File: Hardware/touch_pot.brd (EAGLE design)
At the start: 44.5 x 78.7 mm, 78 parts, among them U1 PIC16F1829, U2 AD5262, U3 5V

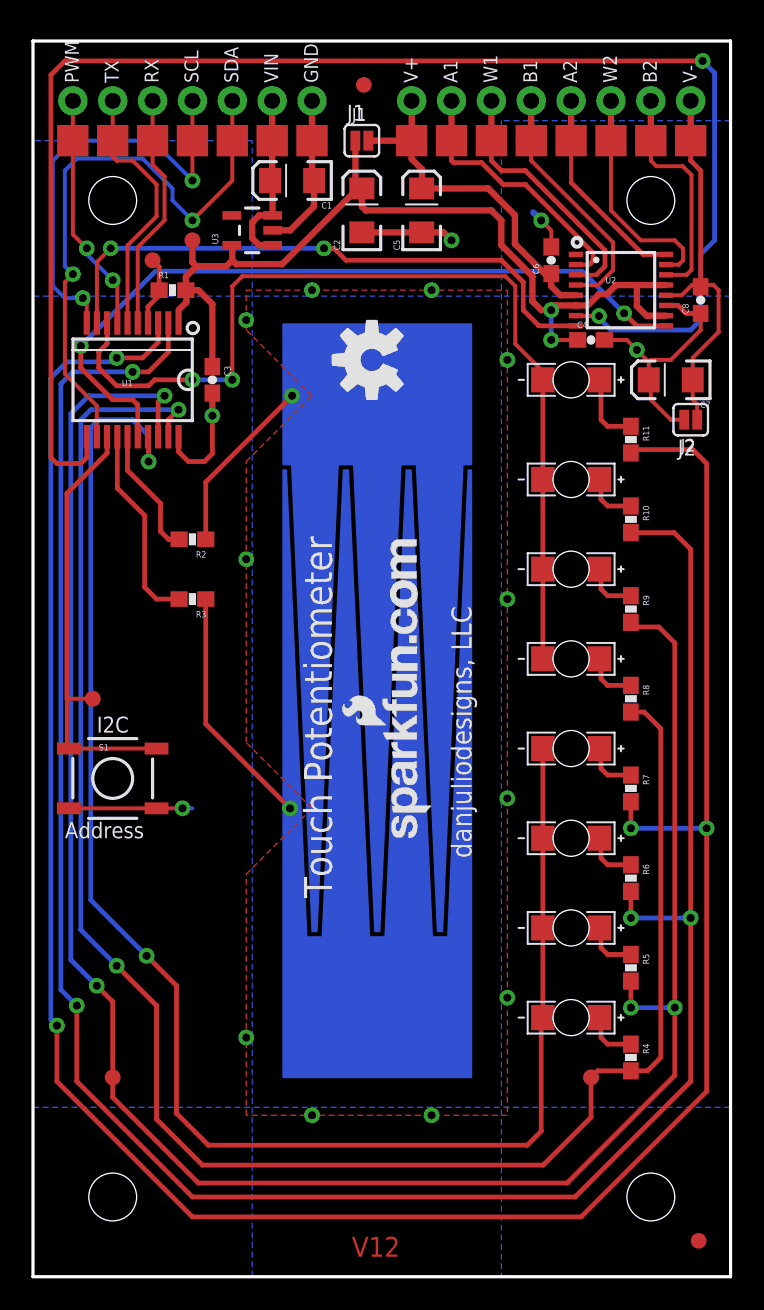
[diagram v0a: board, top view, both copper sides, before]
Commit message: V13 Changes
Adjusted headers to fit on breadboard. Minor rerouting. Moved silk.
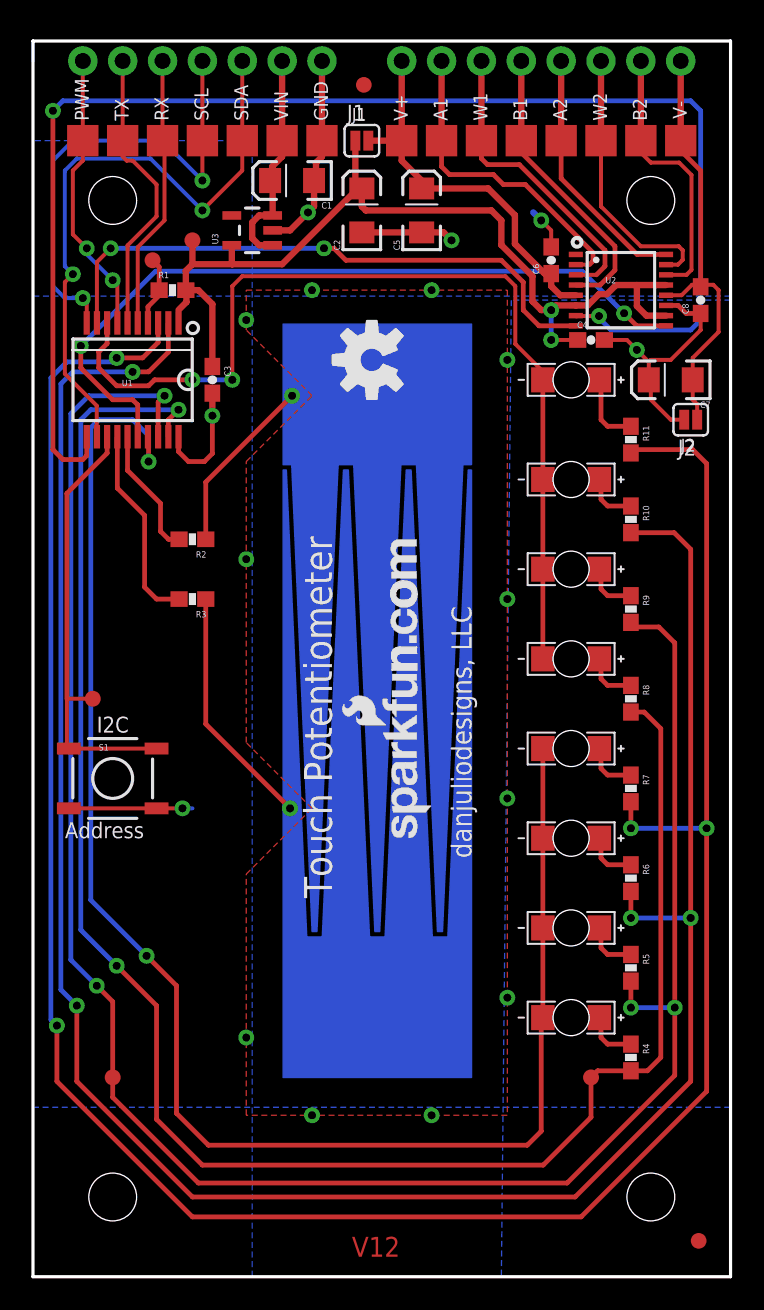
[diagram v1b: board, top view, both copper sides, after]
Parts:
- moved JP1 2.62 mm to (13.3, 77.5)
- moved JP12 2.62 mm to (31.1, 77.5)
- moved JP13 2.62 mm to (28.6, 77.5)
- moved JP14 2.62 mm to (26.0, 77.5)
- moved JP2 2.62 mm to (10.8, 77.5)
- moved JP3 2.62 mm to (3.17, 77.5)
- moved JP4 2.62 mm to (8.26, 77.5)
- moved JP5 2.62 mm to (5.71, 77.5)
- moved JP6 2.62 mm to (15.9, 77.5)
- moved JP10 2.62 mm to (36.2, 77.5)
- moved JP11 2.62 mm to (33.7, 77.5)
- moved JP15 2.62 mm to (23.5, 77.5)
- moved JP7 2.62 mm to (18.4, 77.5)
- moved JP8 2.62 mm to (41.3, 77.5)
- moved JP9 2.62 mm to (38.7, 77.5)
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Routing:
- net SCLK: track 96.1 -> 89.1 mm
- net A1: track 17.0 -> 20.4 mm
- net SCL: track 27.5 -> 30.6 mm
- net W1: track 16.5 -> 19.6 mm
- net A2: track 13.2 -> 16.2 mm
- net B1: track 15.7 -> 18.7 mm
- net W2: track 14.5 -> 17.4 mm
- net B2: track 14.6 -> 17.5 mm
- net GND: track 50.1 -> 52.9 mm, vias 16 -> 17
- net VIN: track 11.4 -> 14.2 mm
- net V-: track 25.0 -> 27.8 mm
- net PWM_OUT: track 15.3 -> 18.1 mm
- net RX: track 15.2 -> 17.5 mm
- net V+: track 22.8 -> 25.0 mm
- net TX: track 16.7 -> 18.6 mm
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
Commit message: V13
v13
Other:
- board text added: "V13"
- board text removed: "V12"
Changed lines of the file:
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@@
 <setting verticaltext="up"/>
 </settings>
-<grid distance="0.05" unitdist="inch" unit="inch" style="lines" multiple="1" display="yes" altdistance="0.005" altunitdist="inch" altunit="inch"/>
+<grid distance="0.05" unitdist="inch" unit="inch" style="lines" multiple="1" display="yes" altdistance="0.0025" altunitdist="inch" altunit="inch"/>
 <layers>
 <layer number="1" name="Top" color="4" fill="1" visible="yes" active="yes"/>
@@
 <text x="19.05" y="24.13" size="1.778" layer="21" ratio="15" rot="R90">Touch Potentiometer</text>
 <text x="27.94" y="26.67" size="1.27" layer="21" ratio="15" rot="R90">danjuliodesigns, LLC</text>
-<text x="13.716" y="73.66" size="0.889" layer="21" ratio="15" rot="R90">SDA</text>
-<text x="11.176" y="73.66" size="0.889" layer="21" ratio="15" rot="R90">SCL</text>
-<text x="3.556" y="73.66" size="0.889" layer="21" ratio="15" rot="R90">PWM</text>
-<text x="6.096" y="73.66" size="0.889" layer="21" ratio="15" rot="R90">TX</text>
-<text x="8.636" y="73.66" size="0.889" layer="21" ratio="15" rot="R90">RX</text>
-<text x="16.256" y="73.66" size="0.889" layer="21" ratio="15" rot="R90">VIN</text>
-<text x="18.796" y="73.66" size="0.889" layer="21" ratio="15" rot="R90">GND</text>
-<text x="23.876" y="73.66" size="0.889" layer="21" ratio="15" rot="R90">V+</text>
-<text x="26.416" y="73.66" size="0.889" layer="21" ratio="15" rot="R90">A1</text>
-<text x="28.956" y="73.66" size="0.889" layer="21" ratio="15" rot="R90">W1</text>
-<text x="31.496" y="73.66" size="0.889" layer="21" ratio="15" rot="R90">B1</text>
-<text x="34.036" y="73.66" size="0.889" layer="21" ratio="15" rot="R90">A2</text>
-<text x="36.576" y="73.66" size="0.889" layer="21" ratio="15" rot="R90">W2</text>
-<text x="39.116" y="73.66" size="0.889" layer="21" ratio="15" rot="R90">B2</text>
-<text x="41.656" y="73.787" size="0.889" layer="21" ratio="15" rot="R90">V-</text>
+<text x="13.716" y="73.914" size="0.889" layer="21" ratio="15" rot="R90">SDA</text>
+<text x="11.176" y="73.914" size="0.889" layer="21" ratio="15" rot="R90">SCL</text>
+<text x="3.683" y="73.914" size="0.889" layer="21" ratio="15" rot="R90">PWM</text>
+<text x="6.096" y="74.7395" size="0.889" layer="21" ratio="15" rot="R90">TX</text>
+<text x="8.6995" y="74.7395" size="0.889" layer="21" ratio="15" rot="R90">RX</text>
+<text x="16.3195" y="74.168" size="0.889" layer="21" ratio="15" rot="R90">VIN</text>
+<text x="18.8595" y="73.914" size="0.889" layer="21" ratio="15" rot="R90">GND</text>
+<text x="23.9395" y="74.7395" size="0.889" layer="21" ratio="15" rot="R90">V+</text>
+<text x="26.416" y="74.7395" size="0.889" layer="21" ratio="15" rot="R90">A1</text>
+<text x="28.956" y="74.7395" size="0.889" layer="21" ratio="15" rot="R90">W1</text>
+<text x="31.496" y="74.7395" size="0.889" layer="21" ratio="15" rot="R90">B1</text>
+<text x="34.036" y="74.7395" size="0.889" layer="21" ratio="15" rot="R90">A2</text>
+<text x="36.576" y="74.7395" size="0.889" layer="21" ratio="15" rot="R90">W2</text>
+<text x="39.116" y="74.7395" size="0.889" layer="21" ratio="15" rot="R90">B2</text>
+<text x="41.656" y="74.7395" size="0.889" layer="21" ratio="15" rot="R90">V-</text>
 <text x="53.34" y="-16.51" size="1.778" layer="51" font="vector" ratio="10">danjuliodesigns, LLC</text>
-<text x="20.32" y="1.27" size="1.27" layer="1" font="vector" ratio="15" distance="45">V12</text>
+<text x="20.32" y="1.27" size="1.27" layer="1" font="vector" ratio="15" distance="45">V13</text>
 <text x="4.064" y="34.671" size="1.016" layer="21" font="vector" ratio="15">I2C</text>
 <text x="2.032" y="27.94" size="1.016" layer="21" font="vector" ratio="15">Address</text>
